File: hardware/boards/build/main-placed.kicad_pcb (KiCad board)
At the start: 4 copper layers, 103 x 84 mm, 146 parts

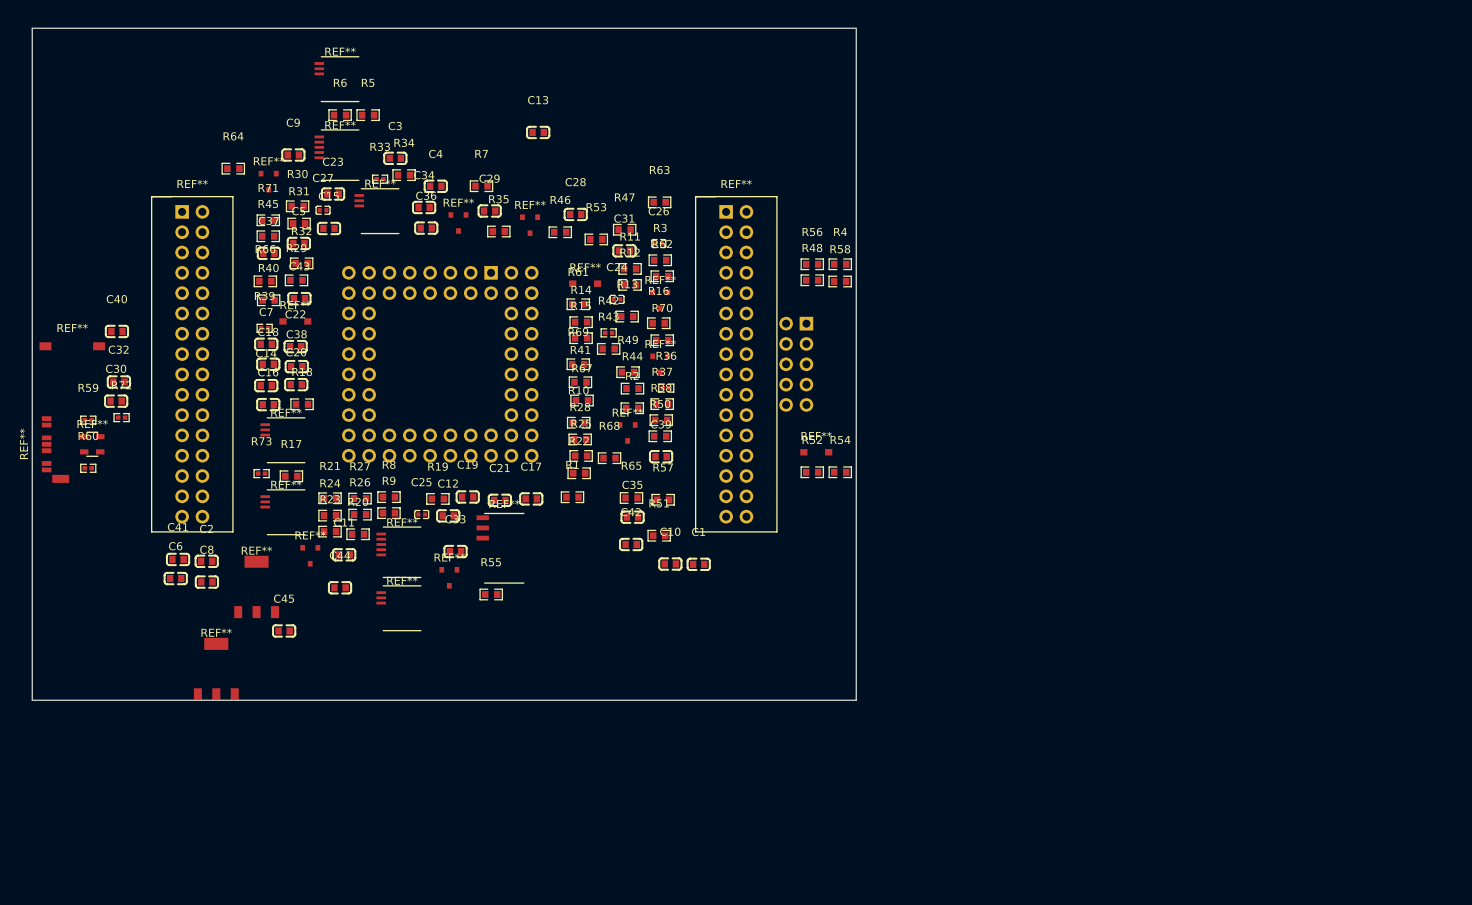
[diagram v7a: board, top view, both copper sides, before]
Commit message: Parts replaced
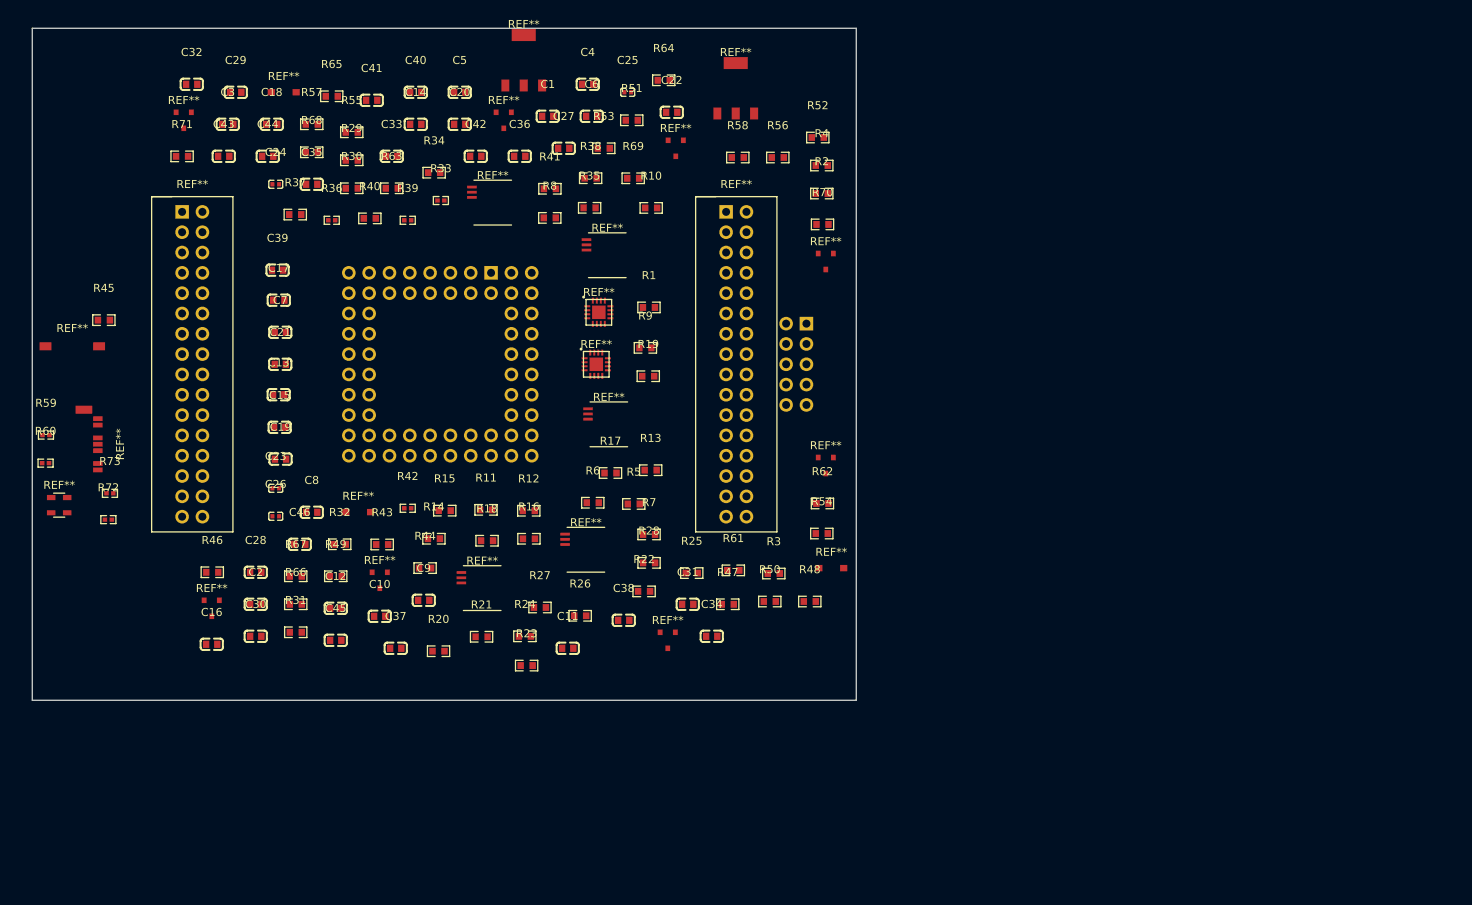
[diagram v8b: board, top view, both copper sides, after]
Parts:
- removed the REF** at (98.0, 53.0)
- removed the REF** at (78.5, 34.0)
- removed the REF** at (46.2, 65.5)
- removed the REF** at (59.0, 65.0)
- removed the REF** at (38.5, 15.9)
- removed the REF** at (46.2, 72.5)
- removed the REF** at (69.1, 31.9)
- removed the REF** at (62.2, 24.6)
- removed the REF** at (31.7, 51.5)
- removed the REF** at (32.9, 36.6)
- removed the REF** at (31.7, 60.5)
- removed the REF** at (43.5, 22.9)
- removed the REF** at (34.7, 65.9)
- removed the REF** at (78.5, 42.0)
- removed the REF** at (38.5, 6.36)
- removed the REF** at (53.3, 24.3)
- removed the REF** at (52.1, 68.7)
- removed the REF** at (29.6, 19.2)
- removed the REF** at (74.4, 50.6)
- added C46: 100nF, YAGEO_CC0603KRX7R9BB104:C0603, F.Cu at (33.4, 64.5)
- added REF**: WQFN-16, DAC80508ZRTER:WQFN-16, F.Cu at (70.5, 42.0)
- added REF**: TSSOP-14, OPA4171AIPWR:TSSOP-14, F.Cu at (69.2, 65.2)
- added REF**: SOD-123, B5819W:SOD-123, F.Cu at (31.4, 8.00)
- added REF**: WQFN-16, DAC80508ZRTER:WQFN-16, F.Cu at (70.8, 35.5)
- added REF**: SOD-123, B5819W:SOD-123, F.Cu at (99.9, 67.5)
- added REF**: SOT-23, 2N3904:SOT-23, F.Cu at (99.2, 54.7)
- added REF**: TSSOP-14, OPA4171AIPWR:TSSOP-14, F.Cu at (57.6, 21.8)
- added REF**: SOT-23, BAT54S:SOT-23, F.Cu at (18.9, 11.5)
- added REF**: SOT-23, BAT54S:SOT-23, F.Cu at (58.9, 11.5)
- added REF**: SOT-23, BAT54S:SOT-23, F.Cu at (80.4, 15.0)
- added REF**: SOT-23, BAT54S:SOT-23, F.Cu at (43.4, 69.0)
- added REF**: TSSOP-14, OPA4171AIPWR:TSSOP-14, F.Cu at (72.1, 49.5)
- added REF**: TSSOP-14, OPA4171AIPWR:TSSOP-14, F.Cu at (71.9, 28.4)
- added REF**: TSSOP-14, OPA4171AIPWR:TSSOP-14, F.Cu at (56.2, 70.0)
- added REF**: SOT-23, BAT54S:SOT-23, F.Cu at (22.4, 72.5)
- added REF**: SOD-123, B5819W:SOD-123, F.Cu at (40.7, 60.5)
- added REF**: SOT-23, 2N3904:SOT-23, F.Cu at (99.2, 29.2)
- added REF**: SOT-23, BAT54S:SOT-23, F.Cu at (79.4, 76.5)
- C1, C11, C13, C14, C15, C16, C17, C18, C19, C2, C20, C21, C22, C3, C30, C33, C36, C4, C41, C42, C43, C44, C45, C5, C6, C9: value 0F -> 100nF
- C10, C12, C38, C39, C7, C8: value 0F -> 10µF
- C23: value 0F -> 1µF; footprint YAGEO_CC0603KRX7R9BB104:C0603 -> Samsung_Electro_Mechanics_CL05A105KA5NQNC:C0402
- C24, C25, C26: value 0F -> 1µF
- C27: value 0F -> 100nF; footprint Samsung_Electro_Mechanics_CL05A105KA5NQNC:C0402 -> YAGEO_CC0603KRX7R9BB104:C0603
- C28, C31, C34, C37: value 0F -> 100nF; footprint Samsung_Electro_Mechanics_CL10A106KP8NNNC:C0603 -> YAGEO_CC0603KRX7R9BB104:C0603
- C29, C32, C35, C40: value 0F -> 10µF; footprint YAGEO_CC0603KRX7R9BB104:C0603 -> Samsung_Electro_Mechanics_CL10A106KP8NNNC:C0603
- R11, R14, R32, R5, R8: value 20000Ω -> 20kΩ
- R12, R15, R17, R18, R20, R21, R23, R24, R26, R27, R29, R31, R34, R37, R40, R43, R45, R46, R47, R49, R51, R53, R55, R57, R6, R63, R64, R65, R66, R67, R68, R71, R9: value 10000Ω -> 10kΩ
- R30: value 15000Ω -> 15kΩ
- R33, R36, R39, R42: value 6040Ω -> 6.04kΩ
- R48, R50, R52, R54, R56, R58: value 22000Ω -> 22kΩ
- R59, R60: value 5100Ω -> 5.1kΩ
- R61, R62, R69, R70: value 1000Ω -> 1kΩ
- moved REF** 86.4 mm to (87.9, 7.50)
- moved REF** 85.3 mm to (61.4, 4.00)
- moved C6 77.7 mm to (69.9, 11.0)
- moved C34 64.5 mm to (84.9, 76.0)
- moved R57 64.3 mm to (34.9, 12.0)
- moved R65 62.7 mm to (37.4, 8.50)
- moved C41 62.3 mm to (42.4, 9.00)
- moved R46 60.8 mm to (22.5, 68.0)
- moved R55 60.4 mm to (39.9, 13.0)
- moved C28 60.0 mm to (27.9, 68.0)
- moved C1 59.1 mm to (64.4, 11.0)
- moved R5 58.9 mm to (75.2, 59.5)
- moved C26 58.8 mm to (30.4, 61.0)
- moved C25 58.7 mm to (74.4, 8.00)
- moved C9 58.0 mm to (48.9, 71.5)
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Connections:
- C10 pad 1: c_lvl-power-hv -> c_dac2_2-power-hv
- C11 pad 1: c_lvl-power-hv -> c_dac2_2-power-hv
- C12 pad 1: c_lvl-power-hv -> c_dac2_2-power-hv
- C13 pad 1: c_lvl-power-hv -> hv
- C13 pad 2: hv -> lv
- C14 pad 1: hv -> c_op5_p-power-hv
- C14 pad 2: lv -> hv
- C15 pad 1: c_op5_p-power-hv -> hv
- C15 pad 2: hv -> lv
- C16 pad 1: hv -> c_op5_p-power-hv
- C16 pad 2: lv -> hv
- C17 pad 1: c_op5_p-power-hv -> hv
- C17 pad 2: hv -> lv
- C18 pad 1: hv -> c_op5_p-power-hv
- C18 pad 2: lv -> hv
- C19 pad 1: c_op5_p-power-hv -> hv
- C19 pad 2: hv -> lv
- C20 pad 1: hv -> c_op5_p-power-hv
- C20 pad 2: lv -> hv
- C21 pad 1: c_op5_p-power-hv -> hv
- C21 pad 2: hv -> lv
- C22 pad 1: hv -> c_op5_p-power-hv
- C22 pad 2: lv -> hv
- C23 pad 1: c_op5_p-power-hv -> c_pitch_ref-power-hv
- C24 pad 1: c_pitch_ref-power-hv -> c_ref1-power-hv
- C25 pad 1: c_ref1-power-hv -> c_ref2-power-hv
- C26 pad 1: c_ref2-power-hv -> c_ref_filt-power-hv
- C27 pad 1: c_ref_filt-power-hv -> c_vio2-power-hv
- C28 pad 1: c_3v3_bulk-power-hv -> c_vio2-power-hv
- C30 pad 1: c_aref-power-hv -> c_3v3_bulk-power-hv
- C31 pad 1: c_vb-power-hv -> c_aref-power-hv
- C32 pad 1: c_lvl-power-hv -> c_vb-power-hv
- C33 pad 1: c_3v3_out_hf-power-hv -> c_dac2_2-power-hv
- C34 pad 1: c_3v3_out_hf-power-hv -> c_vio2-power-hv
- C35 pad 1: c_op5_p-power-hv -> c_vio2-power-hv
- C36 pad 1: c_lvl-power-hv -> c_op5_p-power-hv
- C37 pad 1: c_lvl-power-hv -> c_dac2_2-power-hv
- C38 pad 1: hv -> c_dac2_2-power-hv
- C38 pad 2: lv -> hv
- C39 pad 1: c_op5_p-power-hv -> hv
- C39 pad 2: hv -> lv
- C40 pad 1: c_filter-power-hv -> c_op5_p-power-hv
- C41 pad 1: c_filter-power-hv-1 -> c_filter-power-hv
- C42 pad 1: c_filter-power-hv-2 -> c_filter-power-hv-1
- C43 pad 1: c_filter-power-hv-3 -> c_filter-power-hv-2
- C44 pad 1: c_filter-power-hv-4 -> c_filter-power-hv-3
- C45 pad 1: c_filter-power-hv-5 -> c_filter-power-hv-4
- C9 pad 1: c_lvl-power-hv -> c_dac2_2-power-hv
- R10 pad 1: dac-7-1 -> dac-7-2
- R11 pad 1: dac-8-1 -> dac-8-2
- R12 pad 1: VOUTG -> 7
- R13 pad 1: dac-8-1 -> dac-8-2
- R15 pad 1: VOUTH -> 8
- R20 pad 1: 7 -> dac-7
- R22 pad 1: 7 -> dac-7
- R23 pad 1: 8 -> dac-8
- R25 pad 1: 8 -> dac-8
- R30 pad 1: c_lvl-power-hv -> c_dac2_2-power-hv
- R32 pad 1: c_lvl-power-hv -> c_dac2_2-power-hv
- R36 pad 1: dac-7 -> dac-7-1
- R38 pad 1: dac-7 -> dac-7-1
- R39 pad 1: dac-8 -> dac-8-1
- R41 pad 1: dac-8 -> dac-8-1
- R59 pad 1: 5 -> 5-1
- R6 pad 1: VOUTE -> 5
- R60 pad 1: 6 -> 6-1
- R62 pad 1: c_lvl-power-hv -> c_dac2_2-power-hv
- R63 pad 1: c_3v3_out_hf-power-hv -> c_vio2-power-hv
- R64 pad 1: c_3v3_out_hf-power-hv -> c_vio2-power-hv
- R65 pad 1: c_3v3_out_hf-power-hv -> c_vio2-power-hv
- R66 pad 1: c_3v3_out_hf-power-hv -> c_vio2-power-hv
- R67 pad 1: c_3v3_out_hf-power-hv -> c_vio2-power-hv
- R68 pad 1: c_3v3_out_hf-power-hv -> c_vio2-power-hv
- R70 pad 1: c_lvl-power-hv -> c_dac2_2-power-hv
- R71 pad 1: c_3v3_out_hf-power-hv -> c_vio2-power-hv
- R8 pad 1: dac-7-1 -> dac-7-2
- R9 pad 1: VOUTF -> 6
- REF** pad 2: c_lvl-power-hv -> c_dac2_2-power-hv
- REF** pad 4: c_lvl-power-hv -> c_dac2_2-power-hv (x2)
- REF** pad 3: c_3v3_out_hf-power-hv -> c_vio2-power-hv
- REF** pad 4: c_3v3_out_hf-power-hv -> c_vio2-power-hv (x2)
- REF** pad 5: c_lvl-power-hv -> c_dac2_2-power-hv
- REF** pad 6: c_lvl-power-hv -> c_dac2_2-power-hv
- REF** pad 30: c_lvl-power-hv -> c_dac2_2-power-hv
- REF** pad 2: c_3v3_out_hf-power-hv -> c_vio2-power-hv
- REF** pad 3: c_lvl-power-hv -> c_dac2_2-power-hv
- REF** pad 5: 5 -> 5-1
- REF** pad 6: 6 -> 6-1
- REF** pad 42: spi1_sck -> SCLK
- REF** pad 43: spi1_mosi -> DIN
